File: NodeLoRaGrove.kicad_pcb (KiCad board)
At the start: 2 copper layers, 42 parts, among them P1 PICKIT PROGRAMMER, P2 USB_A, P3 CONN_01X02, P4 GROVE 2, P5 GROVE 4, P6 GROVE 1, P7 GROVE 3, SW1 SW_PUSH, U1 AP2112, U2 MCP73831T-2ATI/OT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

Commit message: Add PCB 0.8v
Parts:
- A1, C4, C5, MODULE1, R1, R13, R14, R2, R3, R6: moved to B.Cu
- moved A1 108.9 mm to (121.3, 55.4), turned to 270 degrees
- moved P6 86.3 mm to (107.0, 86.5), turned to 270 degrees
- moved R5 85.9 mm to (103.4, 65.2)
- moved U2 82.9 mm to (106.5, 74.3), turned to 270 degrees
- moved P4 80.4 mm to (104.0, 98.0)
- moved SW1 75.6 mm to (109.8, 58.0), turned to 90 degrees
- moved R7 74.6 mm to (102.8, 74.5), turned to 270 degrees
- moved U1 73.9 mm to (103.5, 69.0), turned to 270 degrees
- moved D1 73.4 mm to (103.3, 61.9), turned to 180 degrees
- moved P3 71.8 mm to (101.9, 56.9), turned to 90 degrees
- moved R6 66.6 mm to (131.4, 75.8), turned to 90 degrees
- moved D7 57.5 mm to (108.4, 80.3), turned to 270 degrees
- moved C6 57.1 mm to (103.1, 80.2), turned to 270 degrees
- moved C9 56.7 mm to (124.5, 66.8)
- moved C1 56.0 mm to (108.7, 61.9)
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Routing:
- net VCC: track 0.00 -> 167.5 mm, vias 0 -> 5
- net +3V3: track 0.00 -> 133.9 mm, vias 0 -> 8
- net GND: track 0.00 -> 108.1 mm, vias 0 -> 17
- net /SCL: track 0.00 -> 45.2 mm, vias 0 -> 1
- net /D13: track 0.00 -> 32.8 mm, vias 0 -> 1
- net +BATT: track 0.00 -> 31.2 mm
- net /SDA: track 0.00 -> 29.5 mm, vias 0 -> 3
- net Net-(MODULE1-Pad35): track 0.00 -> 28.6 mm, vias 0 -> 2
- net /D6: track 0.00 -> 27.4 mm, vias 0 -> 2
- net /D9: track 0.00 -> 27.0 mm, vias 0 -> 2
- net Net-(R11-Pad1): track 0.00 -> 26.9 mm
- net /RST: track 0.00 -> 25.6 mm, vias 0 -> 2
- net Net-(MODULE1-Pad36): track 0.00 -> 24.5 mm
- net /A3: track 0.00 -> 22.4 mm
- net /RST_RN: track 0.00 -> 22.4 mm, vias 0 -> 1
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- added copper zone on B.Cu, net GND
- added copper zone on F.Cu, net GND
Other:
- board outline added: 40 x 50 mm
- net class Default: trace_width 0.25 -> 0.3
- net class Vcc added: clearance 0.2, trace_width 0.5, via_dia 0.6, via_drill 0.4

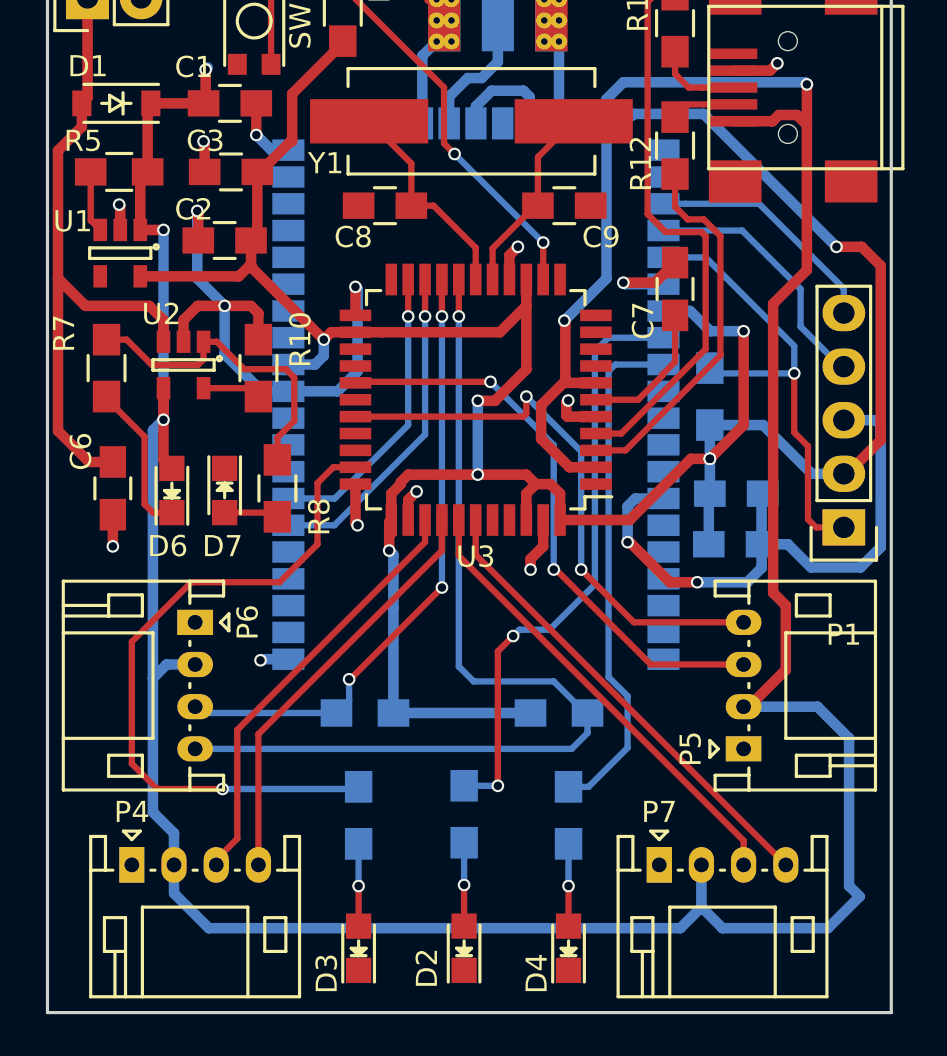
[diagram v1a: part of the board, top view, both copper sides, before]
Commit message: Update labels and added logo ElectronicCats
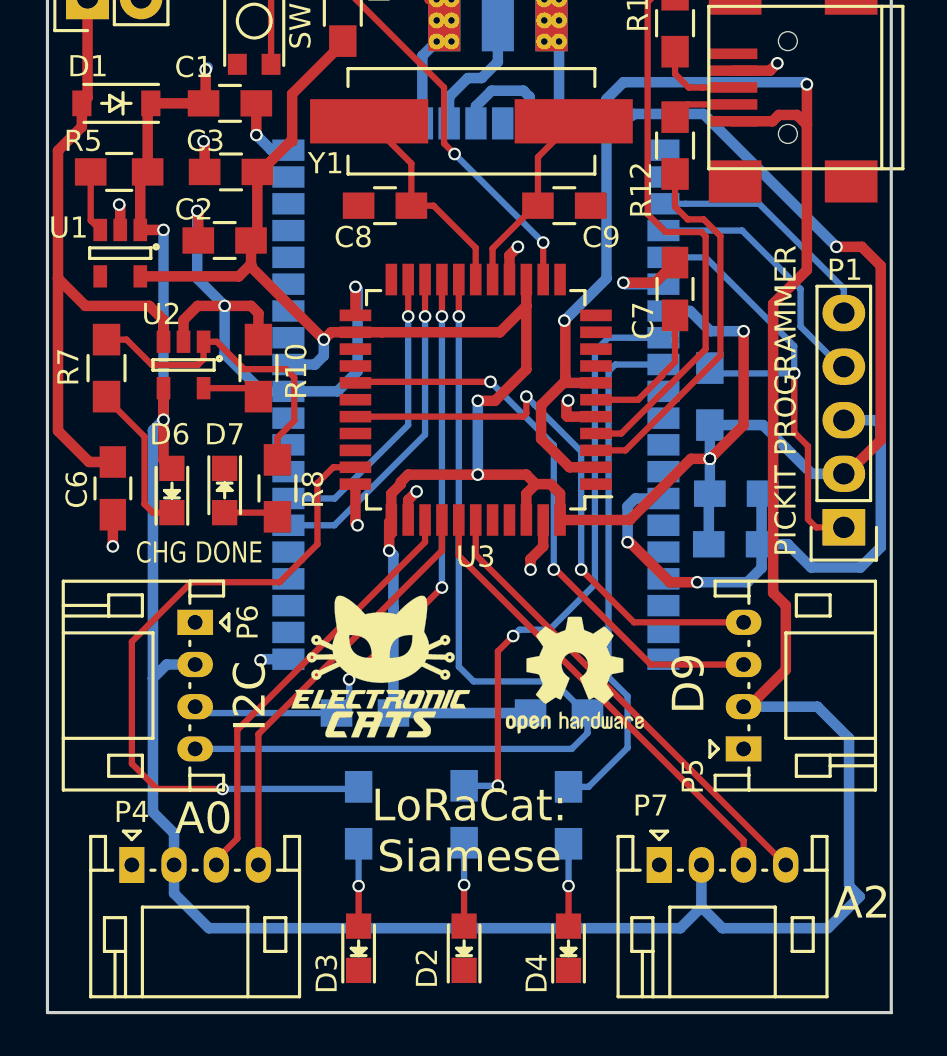
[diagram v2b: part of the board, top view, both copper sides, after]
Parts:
- added G***: LOGO, TIH:electronic_cats_logo_8x6, F.Cu at (115.8, 88.6)
- added REF***: OSHW-Logo2_7.3x6mm_SilkScreen, Symbols:OSHW-Logo2_7.3x6mm_SilkScreen, F.Cu at (125.0, 89.0)
- added REF***: FCC-Logo_7.3x6mm_SilkScreen, Symbols:FCC-Logo_7.3x6mm_SilkScreen, B.Cu at (104.4, 75.6)
- D6: value Led_Small -> CHG
- D7: value Led_Small -> DONE
- P3: value CONN_01X02 -> Battery
- P4: value GROVE 2 -> A0
- P5: value GROVE 4 -> D9
- P6: value GROVE 1 -> I2C
- P7: value GROVE 3 -> A2
- R7: value 1K -> 330R
- R8: value R_Small -> 330R
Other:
- board text added: "D9 D6 VCC GND"
- board text added: "GND VCC A0 A1"
- board text added: "GND VCC A2 A3"
- board text added: "GND VCC SDA SCL"
- board text added: "LoRaCat: Siamese"

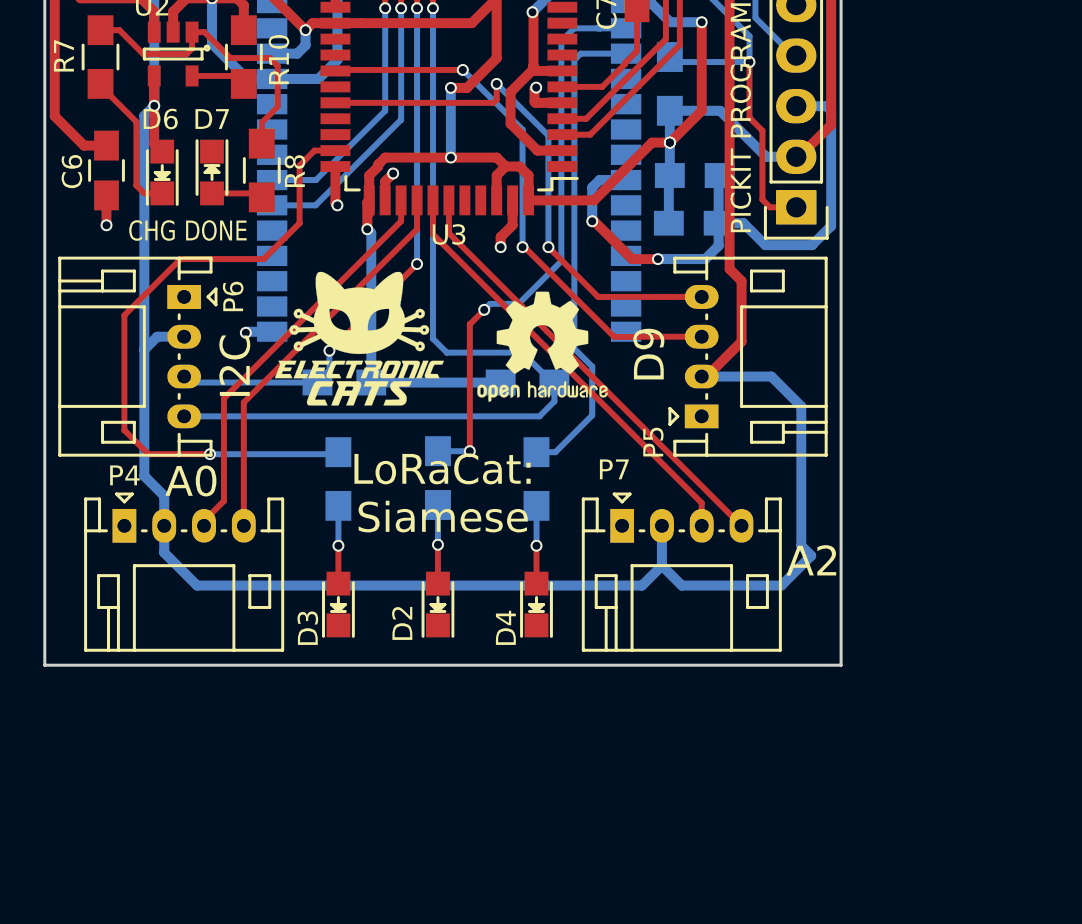
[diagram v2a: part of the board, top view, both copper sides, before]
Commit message: Update Schematic remove leds
Notes and leds remove
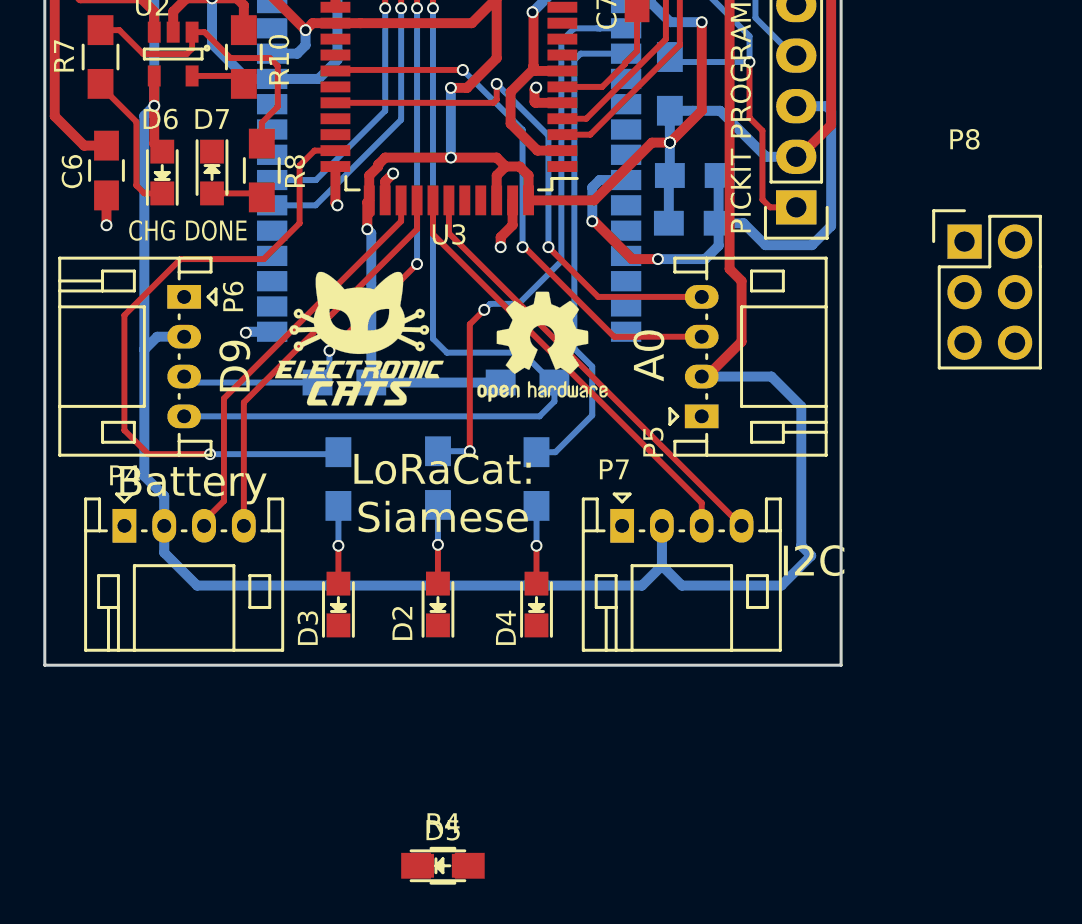
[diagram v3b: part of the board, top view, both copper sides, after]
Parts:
- added D5: LED, LEDs:LED_0805, F.Cu at (120.0, 115.1)
- added P8: A2, Pin_Headers:Pin_Header_Straight_2x03, F.Cu at (146.2, 83.7)
- added R4: 330R, Resistors_SMD:R_0805_HandSoldering, F.Cu at (120.0, 115.1)
- D3: value LED -> CHG
- D4: value Led -> DONE
- P2: value USB_A -> ICSP
- P3: value Battery -> USB_A
- P4: value A0 -> Battery
- P5: value D9 -> A0
- P6: value I2C -> D9
- P7: value A2 -> I2C
- R10, R9: value 10K -> 22R
- R11, R12: value 22R -> 4.7K
- R2: value 330 -> 100K
- R3: value 100R -> 10K
- R5: value 100K -> 330R
- R6: value 10K -> 330
- R7, R8: value 330R -> 10K
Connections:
- D3 pad 1: GND -> Net-(D3-Pad1)
- D3 pad 2: Net-(D3-Pad2) -> VCC
- P2 pad 1: VCC -> GND
- P2 pad 2: /D- -> /RST
- P2 pad 3: /D+ -> /MOSI
- P2 pad 4: GND -> /SCK
- P2 pad 5: Net-(P2-Pad5) -> VCC
- P2 pad 6: (no net) -> /MISO
- P3 pad 1: +BATT -> VCC
- P3 pad 2: GND -> /D-
- P4 pad 1: GND -> +BATT
- P4 pad 2: VCC -> GND
- P4 pad 3: /A0 -> (no net)
- P4 pad 4: /A1 -> (no net)
- P5 pad 3: /D6 -> /A0
- P5 pad 4: /D9 -> /A1
- P6 pad 3: /SDA -> /D6
- P6 pad 4: /SCL -> /D9
- P7 pad 3: /A2 -> /SDA
- P7 pad 4: /A3 -> /SCL
- R1 pad 1: Net-(MODULE1-Pad35) -> Net-(MODULE1-Pad36)
- R10 pad 2: GND -> /D-
- R11 pad 1: Net-(R11-Pad1) -> +3V3
- R11 pad 2: /D+ -> /SDA
- R12 pad 1: Net-(R12-Pad1) -> +3V3
- R12 pad 2: /D- -> /SCL
- R2 pad 1: /D13 -> Net-(R2-Pad1)
- R2 pad 2: Net-(D3-Pad2) -> VCC
- R3 pad 1: Net-(MODULE1-Pad36) -> +3V3
- R3 pad 2: Net-(D4-Pad2) -> /RST_RN
- R5 pad 1: Net-(R5-Pad1) -> Net-(R4-Pad1)
- R5 pad 2: VCC -> Net-(D4-Pad2)
- R6 pad 1: +3V3 -> /D13
- R6 pad 2: /RST_RN -> Net-(D5-Pad2)
- R7 pad 1: Net-(R7-Pad1) -> +3V3
- R7 pad 2: Net-(D6-Pad1) -> /RST
- R8 pad 1: Net-(R7-Pad1) -> Net-(R8-Pad1)
- R8 pad 2: Net-(D7-Pad2) -> GND
- R9 pad 1: +3V3 -> Net-(R9-Pad1)
- R9 pad 2: /RST -> /D+
- U1 pad 3: Net-(R5-Pad1) -> Net-(R2-Pad1)
- U2 pad 1: Net-(R7-Pad1) -> Net-(R4-Pad1)
- U2 pad 5: Net-(R10-Pad1) -> Net-(R8-Pad1)
- U3 pad 10: Net-(U3-Pad10) -> /MOSI
- U3 pad 11: Net-(U3-Pad11) -> /MISO
- U3 pad 3: Net-(R12-Pad1) -> Net-(R10-Pad1)
- U3 pad 4: Net-(R11-Pad1) -> Net-(R9-Pad1)
- U3 pad 9: Net-(U3-Pad9) -> /SCK
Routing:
- net VCC: track 167.5 -> 66.3 mm, vias 5 -> 3
- net GND: track 108.1 -> 206.4 mm, vias 17 -> 19
- net +3V3: track 133.9 -> 178.4 mm
- net Net-(R2-Pad1): track 0.00 -> 31.3 mm, vias 0 -> 1
- net /D13: track 32.8 -> 4.86 mm, vias 1 -> 0
- net Net-(R11-Pad1): track 26.9 -> 0.00 mm
- net /A0: track 20.5 -> 41.5 mm, vias 0 -> 1
- net /A3: track 22.4 -> 1.65 mm
- net /A2: track 21.9 -> 1.60 mm
- net Net-(R12-Pad1): track 17.7 -> 0.00 mm
- net /SDA: track 29.5 -> 45.6 mm
- net Net-(R7-Pad1): track 15.3 -> 0.00 mm
- net /D6: track 27.4 -> 13.2 mm, vias 2 -> 1
- net /D+: track 4.07 -> 16.2 mm, vias 0 -> 1
- net Net-(R4-Pad1): track 0.00 -> 11.3 mm
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
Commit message: Added PCB 0.9v
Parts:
- removed D6: CHG, LEDs:LED_0805
- removed D7: DONE, LEDs:LED_0805
- removed G***: LOGO, TIH:electronic_cats_logo_8x6
- removed R13, R14: 4.7K, Resistors_SMD:R_0805_HandSoldering
- removed REF***: OSHW-Logo2_7.3x6mm_SilkScreen, Symbols:OSHW-Logo2_7.3x6mm_SilkScreen
- removed REF***: FCC-Logo_7.3x6mm_SilkScreen, Symbols:FCC-Logo_7.3x6mm_SilkScreen
- A1: footprint TIH:GSG-SMA-EDGE -> CatSat:SMA_Conn_Ant
- C1, C2, C3, D1, P1, R11, R12, U1: moved to B.Cu
- MODULE1: footprint modules:RN2483 -> Library:RN2483
- P2: footprint Connect:USB_Mini-B -> Pin_Headers:Pin_Header_Straight_2x03
- P3: footprint Pin_Headers:Pin_Header_Straight_1x02 -> Connect:USB_Mini-B
- P4: footprint Connectors_JST:JST_PH_S4B-PH-K_04x2.00mm_Angled -> Pin_Headers:Pin_Header_Straight_1x02
- P8: footprint Pin_Headers:Pin_Header_Straight_2x03 -> Connectors_JST:JST_PH_S4B-PH-K_04x2.00mm_Angled
- R1, R6: moved to F.Cu
- SW1: footprint TIH:SW_SPST_KMR2 -> modules:SW_SPST_KMR2
- U2: value MCP73831T-2ATI/OT -> MCP73831T
- moved R4 44.6 mm to (109.2, 71.8), turned to 180 degrees
- moved P4 43.4 mm to (106.7, 54.7), turned to 180 degrees
- moved P3 38.2 mm to (140.1, 55.8), turned to 180 degrees
- moved P8 35.9 mm to (111.5, 93.0)
- moved R3 35.2 mm to (138.7, 63.4)
- moved D4 29.0 mm to (113.5, 75.2)
- moved R10 28.3 mm to (132.1, 56.7), turned to 0 degrees
- moved R11 28.1 mm to (122.5, 85.2), turned to 90 degrees
- moved C4 27.4 mm to (110.2, 64.7), turned to 180 degrees
- moved D3 27.2 mm to (109.7, 75.2)
- moved P2 26.3 mm to (110.5, 54.7), turned to 90 degrees
- moved C5 25.3 mm to (138.7, 58.2), turned to 90 degrees
- moved R2 22.6 mm to (110.1, 73.5)
- moved R12 21.5 mm to (127.5, 85.2)
- moved D5 18.8 mm to (122.5, 96.5), turned to 90 degrees
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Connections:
- A1 pad 4: GND -> (no net)
- A1 pad 5: GND -> (no net)
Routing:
- net VCC: track 66.3 -> 158.1 mm, vias 3 -> 5
- net /A2: track 1.60 -> 76.3 mm, vias 0 -> 1
- net /A3: track 1.65 -> 73.9 mm, vias 0 -> 2
- net GND: track 206.4 -> 135.9 mm, vias 19 -> 18
- net +3V3: track 178.4 -> 142.7 mm, vias 8 -> 7
- net Net-(R2-Pad1): track 31.3 -> 3.19 mm, vias 1 -> 0
- net /D13: track 4.86 -> 32.7 mm
- net Net-(MODULE1-Pad35): track 19.6 -> 0.00 mm, vias 1 -> 0
- net /SCK: track 2.24 -> 19.8 mm, vias 1 -> 0
- net /RST: track 15.2 -> 30.2 mm, vias 1 -> 0
- net /SCL: track 50.1 -> 36.2 mm
- net Net-(C9-Pad1): track 9.17 -> 22.7 mm, vias 0 -> 2
- net /MISO: track 0.00 -> 13.2 mm
- net /D6: track 13.2 -> 25.4 mm
- net /D+: track 16.2 -> 4.20 mm, vias 1 -> 0
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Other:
- board text removed: "D9 D6 VCC GND"
- board text removed: "GND VCC A0 A1"
- board text removed: "GND VCC A2 A3"
- board text removed: "GND VCC SDA SCL"
- board text removed: "LoRaCat: Siamese"

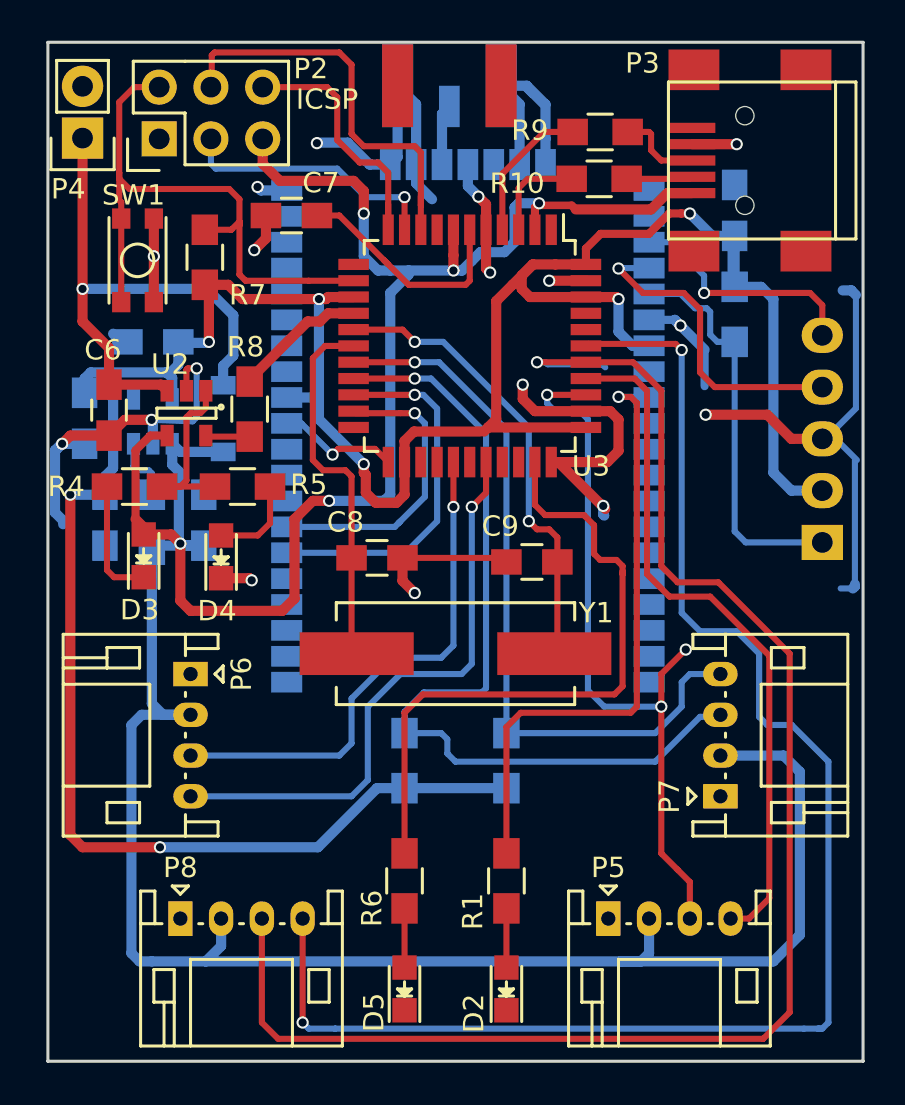
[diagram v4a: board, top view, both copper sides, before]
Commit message: Added logos and change button
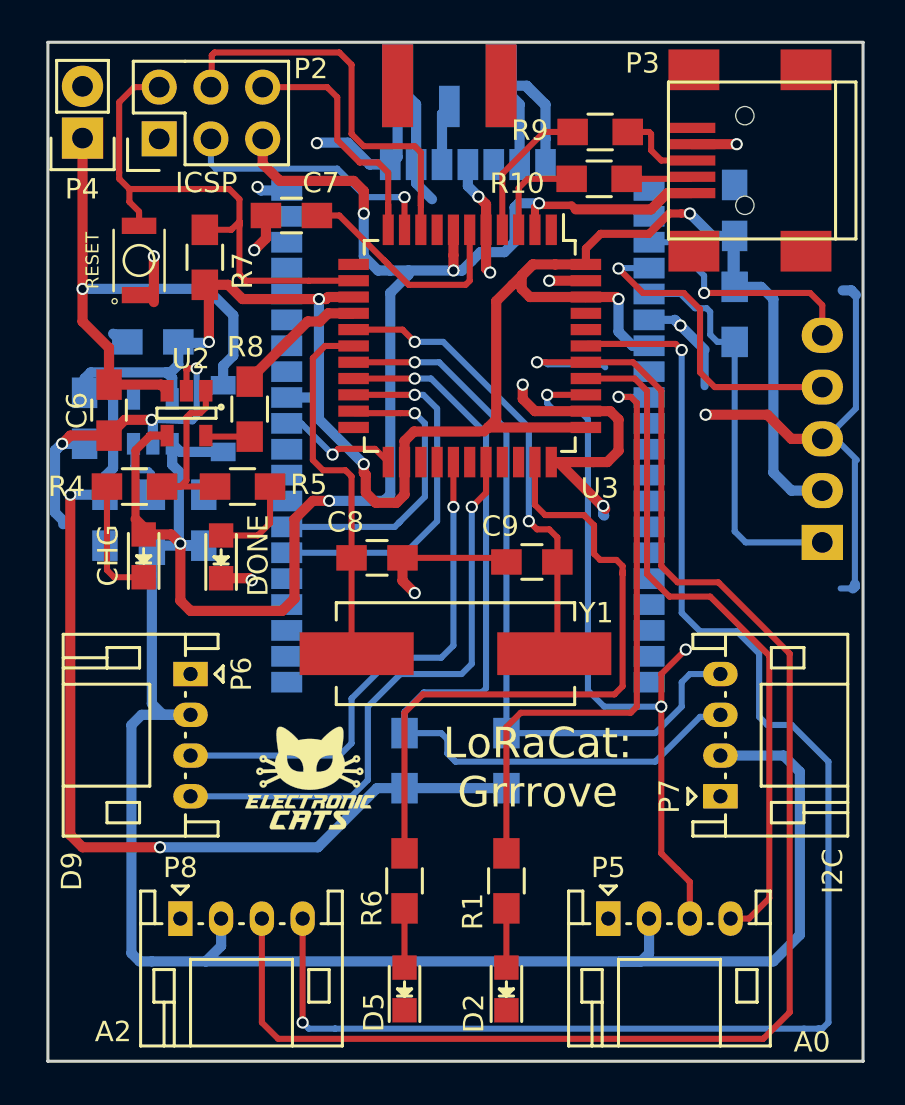
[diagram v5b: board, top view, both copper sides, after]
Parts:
- added G***: LOGO, TIH:electronic_cats_logo_4x3, F.Cu at (117.9, 86.1)
- added REF***: OSHW-Logo2_7.3x6mm_SilkScreen, Symbols:OSHW-Logo2_7.3x6mm_SilkScreen, B.Cu at (125.0, 93.2)
- P4: value Battery -> - Battery +
- SW1: value SW_PUSH -> RESET; footprint modules:SW_SPST_KMR2 -> TIH:SW_B3U-1000P
- U2: value MCP73831T -> MCP73831T-2ATI/OT
- moved SW1 0.07 mm to (109.5, 60.7), turned to 90 degrees
- renumbered MODULE1 to RN2903
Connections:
- A1 pad 4: (no net) -> GND
- A1 pad 5: (no net) -> GND
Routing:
- net /RST: track 30.2 -> 25.8 mm
- net GND: track 135.9 -> 134.1 mm
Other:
- board text added: "GND VCC A0 A1"
- board text added: "GND VCC A2 A3"
- board text added: "GND VCC D6 D9"
- board text added: "GND VCC SDA SCL"
- board text added: "LoRaCat: Grrrove"

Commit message: Check DRC PCB
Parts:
- moved C9 32.0 mm to (148.6, 100.7)
- moved D2 32.0 mm to (147.3, 121.6)
- moved D5 32.0 mm to (142.3, 121.6)
- moved G*** 32.0 mm to (137.7, 111.3)
- moved P5 32.0 mm to (152.3, 118.2)
- moved P6 32.0 mm to (131.8, 106.2)
- moved P7 32.0 mm to (157.8, 112.2)
- moved P8 32.0 mm to (131.3, 118.2)
- moved R11 32.0 mm to (142.3, 110.4)
- moved R12 32.0 mm to (147.3, 110.4)
- moved R2 32.0 mm to (129.9, 98.7)
- moved R3 32.0 mm to (158.5, 88.5)
- moved R4 32.0 mm to (129.1, 97.0)
- moved Y1 32.0 mm to (144.8, 105.2)
- moved A1 32.0 mm to (144.5, 75.2)
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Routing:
- net GND: track 134.1 -> 143.6 mm, vias 18 -> 19
- net /A2: track 76.3 -> 70.4 mm, vias 1 -> 0
- net +3V3: track 142.7 -> 146.6 mm
- net /D+: track 4.20 -> 5.58 mm
- net Net-(R9-Pad1): track 7.05 -> 7.94 mm
- net /D-: track 3.24 -> 3.93 mm
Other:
- board text added: "SCL SDA VCC GND"
- board text removed: "GND VCC SDA SCL"
